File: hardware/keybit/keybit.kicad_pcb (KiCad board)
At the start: 2 copper layers, 19 x 19 mm, 23 parts, among them SW1 SW_Push, U1 CH32V003FxUx, U2 YZ13515055F-02025-02, U3 YZ13515055F-02025-02, U4 YZ13515055F-02025-02, U5 YZ13515055F-02025-02, U6 YZ13515055F-02025-02, U7 YZ13515055F-02025-02, U8 YZ13515055F-02025-02, U9 YZ13515055F-02025-02

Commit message: finish case and stuff
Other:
- outline, holes or cut-outs redrawn
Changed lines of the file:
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@@
 		)
 	)
-	(gr_rect
-		(start 140.49375 66.65)
-		(end 159.54375 85.7)
+	(gr_line
+		(start 159.54375 68.65)
+		(end 159.54375 83.7)
 		(stroke
 			(width 0.05)
-			(type solid)
+			(type default)
 		)
-		(fill no)
 		(layer "Edge.Cuts")
 	)
+	(gr_line
+		(start 142.49375 66.65)
+		(end 157.54375 66.65)
+		(stroke
+			(width 0.05)
+			(type default)
+		)
+		(layer "Edge.Cuts")
+	)
+	(gr_line
+		(start 157.54375 85.7)
+		(end 142.49375 85.7)
+		(stroke
+			(width 0.05)
+			(type default)
+		)
+		(layer "Edge.Cuts")
+	)
+	(gr_line
+		(start 140.49375 83.7)
+		(end 140.49375 68.65)
+		(stroke
+			(width 0.05)
+			(type default)
+		)
+		(layer "Edge.Cuts")
+	)
+	(gr_arc
+		(start 157.54375 66.65)
+		(mid 158.957964 67.235786)
+		(end 159.54375 68.65)
+		(stroke
+			(width 0.05)
+			(type default)
+		)
+		(layer "Edge.Cuts")
+	)
+	(gr_arc
+		(start 159.54375 83.7)
+		(mid 158.957964 85.114214)
+		(end 157.54375 85.7)
+		(stroke
+			(width 0.05)
+			(type default)
+		)
+		(layer "Edge.Cuts")
+	)
+	(gr_arc
+		(start 140.49375 68.65)
+		(mid 141.079539 67.235804)
+		(end 142.49375 66.65)
+		(stroke
+			(width 0.05)
+			(type default)
+		)
+		(layer "Edge.Cuts")
+	)
+	(gr_arc
+		(start 142.49375 85.7)
+		(mid 141.079536 85.114214)
+		(end 140.49375 83.7)
+		(stroke
+			(width 0.05)
+			(type default)
+		)
+		(layer "Edge.Cuts")
+	)

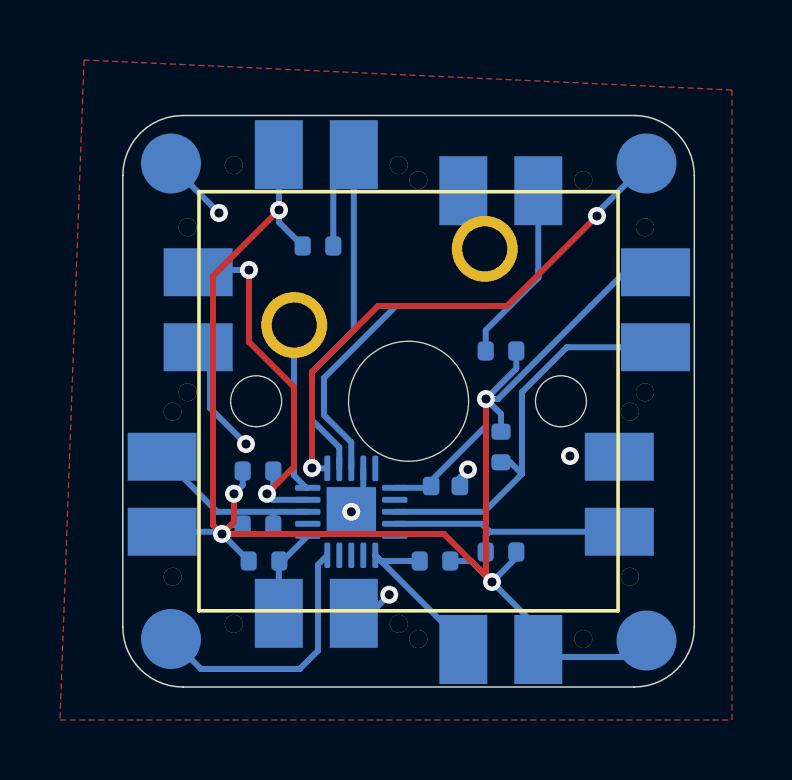
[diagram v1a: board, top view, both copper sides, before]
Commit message: add in mousebites
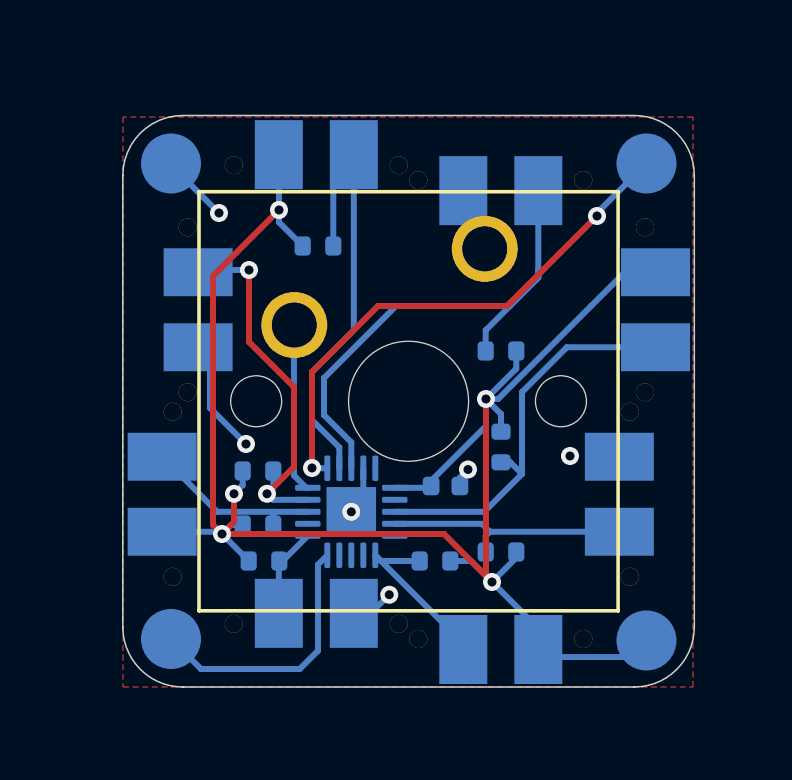
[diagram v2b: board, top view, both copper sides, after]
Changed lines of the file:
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@@
 		(polygon
 			(pts
-				(xy 160.8 86.8) (xy 160.8 65.8) (xy 139.2 64.8) (xy 138.4 86.8)
+				(xy 159.5 85.7) (xy 159.5 66.7) (xy 140.5 66.7) (xy 140.5 85.7)
 			)
 		)

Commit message: blender and stuff
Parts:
- moved TP1 0.25 mm to (157.8, 84.0)
- moved TP3 0.22 mm to (157.8, 68.4)
- moved TP4 0.21 mm to (142.2, 68.4)
- moved TP2 0.21 mm to (142.2, 84.0)
